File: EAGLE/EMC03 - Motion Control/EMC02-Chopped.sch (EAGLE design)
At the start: 153 parts, among them IC1 74ACT244DW, IC2 74ACT244DW, J1 CONN-0.1-S-1X3, J10 UART0, J11 HR911105A, J12 USD-SOCKETSMD, J13 USB-B, J14 SWD, J17 CONN-0.1-S-1X3, J18 CONN-0.1-S-2X3, J19 CONN-0.1-S-2X3, J2 CONN-0.1-S-1X3, J20 CONN-0.1-S-2X3, J22A OSTTH050160, J3 CONN-0.1-S-1X3, J31 CONN-0.1-S-1X2, J4 CONN-0.1-RA-1X4, J4A MOT-X, J5 CONN-0.1-RA-1X4, J5A MOT-Y, J6 CONN-0.1-RA-1X4, J6A MOT-Z, J7 CONN-0.1-RA-1X3, J7A CONN-RECT-3PINJST_PH_2MM, J8 CONN-0.1-RA-1X3, J8A CONN-RECT-3PINJST_PH_2MM, J9 CONN-0.1-RA-1X3, J9A CONN-RECT-3PINJST_PH_2MM, Q1 25MHz, U1 LPC1768, U2 SP3485, U3 CPL-ETH-PHY-LAN8720A, U4 74LVC1G04, U5 TC1015-3.3VCT713

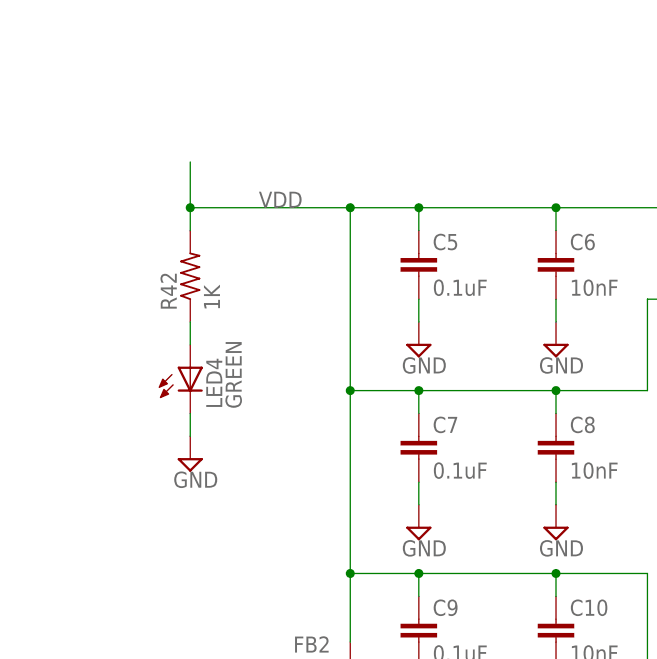
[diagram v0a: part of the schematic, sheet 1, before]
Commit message: Began integration into EMC02 legacy schematic. Unnecessary components removed from EMC02. MCU, peripherals added to the EMC02 schematic. Schematic renamed EMC03-Motion Control. LEDs added, switching regulator LM2576-5.0 picked, modeled.
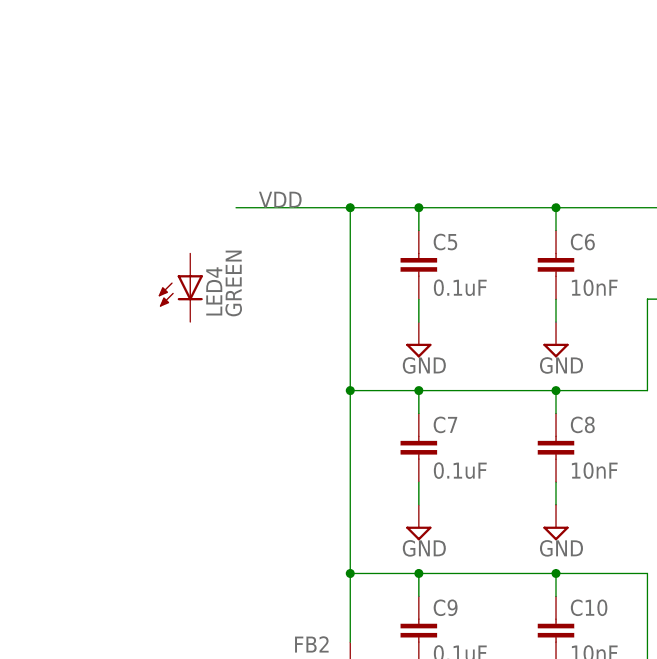
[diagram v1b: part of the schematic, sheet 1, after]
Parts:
- removed R42: 1K, TinWhiskers:CPL-RES-0603-1K-0.1W
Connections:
- removed net N$9: LED4.A, R42.1
- net GND: no longer LED4.C
- net VDD: no longer R42.2
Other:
- moved on the sheet: LED4
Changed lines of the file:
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@@
 <part name="RJ1" library="TinWhiskers" deviceset="CPL-CON-MOD-RJ45" device="" value="RJ-45"/>
 <part name="SUPPLY39" library="TinWhiskers" deviceset="GND" device=""/>
-<part name="R42" library="TinWhiskers" deviceset="CPL-RES-0603-1K-0.1W" device="" value="1K"/>
-<part name="SUPPLY40" library="TinWhiskers" deviceset="GND" device=""/>
 </parts>
 <sheets>
@@
 </instance>
 <instance part="SUPPLY34" gate="GND" x="314.96" y="116.84"/>
-<instance part="LED4" gate="G$1" x="22.86" y="170.18" smashed="yes">
-<attribute name="NAME" x="26.416" y="165.608" size="1.778" layer="95" rot="R90"/>
-<attribute name="VALUE" x="28.575" y="165.608" size="1.778" layer="96" rot="R90"/>
+<instance part="LED4" gate="G$1" x="22.86" y="180.34" smashed="yes">
+<attribute name="NAME" x="26.416" y="175.768" size="1.778" layer="95" rot="R90"/>
+<attribute name="VALUE" x="28.575" y="175.768" size="1.778" layer="96" rot="R90"/>
 </instance>
 <instance part="LED5" gate="G$1" x="274.32" y="241.3" smashed="yes">
@@
 </instance>
 <instance part="SUPPLY38" gate="GND" x="299.72" y="170.18"/>
-<instance part="R42" gate="G$1" x="22.86" y="180.34" smashed="yes" rot="R90">
-<attribute name="NAME" x="21.3614" y="176.53" size="1.778" layer="95" rot="R90"/>
-<attribute name="VALUE" x="26.162" y="176.53" size="1.778" layer="96" rot="R90"/>
-</instance>
-<instance part="SUPPLY40" gate="GND" x="22.86" y="160.02"/>
 </instances>
 <busses>
@@
 <wire x1="299.72" y1="172.72" x2="299.72" y2="175.26" width="0.1524" layer="91"/>
 </segment>
-<segment>
-<pinref part="LED4" gate="G$1" pin="C"/>
-<pinref part="SUPPLY40" gate="GND" pin="GND"/>
-<wire x1="22.86" y1="165.1" x2="22.86" y2="162.56" width="0.1524" layer="91"/>
-</segment>
 </net>
 <net name="VDD" class="0">
@@
 <junction x="48.26" y="187.96"/>
 <label x="99.06" y="182.88" size="1.778" layer="95"/>
-<wire x1="40.64" y1="187.96" x2="22.86" y2="187.96" width="0.1524" layer="91"/>
+<wire x1="40.64" y1="187.96" x2="27.94" y2="187.96" width="0.1524" layer="91"/>
 <junction x="40.64" y="187.96"/>
 <pinref part="U1" gate="G$1" pin="VDD@96"/>
@@
 <junction x="40.64" y="147.32"/>
 <label x="30.48" y="187.96" size="1.778" layer="95"/>
-<wire x1="22.86" y1="187.96" x2="22.86" y2="193.04" width="0.1524" layer="91"/>
-<pinref part="R42" gate="G$1" pin="2"/>
-<wire x1="22.86" y1="185.42" x2="22.86" y2="187.96" width="0.1524" layer="91"/>
-<junction x="22.86" y="187.96"/>
 </segment>
 </net>
@@
 </segment>
 </net>
-<net name="N$9" class="0">
-<segment>
-<pinref part="LED4" gate="G$1" pin="A"/>
-<pinref part="R42" gate="G$1" pin="1"/>
-<wire x1="22.86" y1="172.72" x2="22.86" y2="175.26" width="0.1524" layer="91"/>
-</segment>
-</net>
